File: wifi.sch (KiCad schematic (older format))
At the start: 5 parts

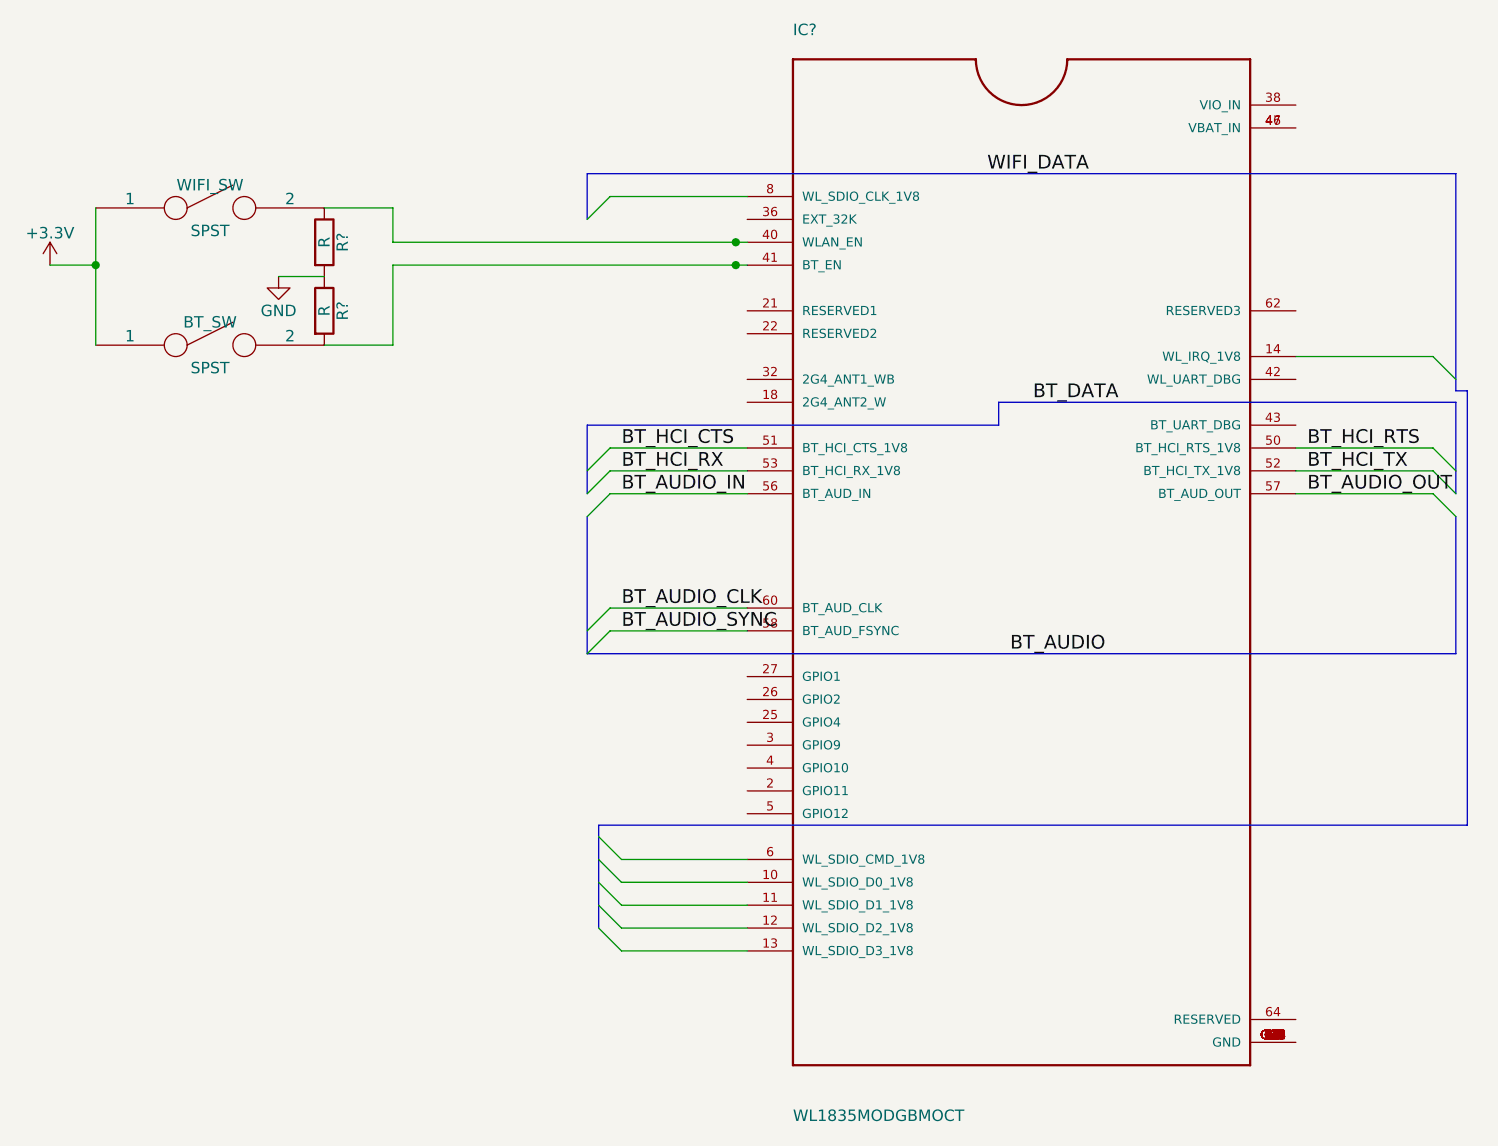
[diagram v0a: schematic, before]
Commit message: modular concept sketch
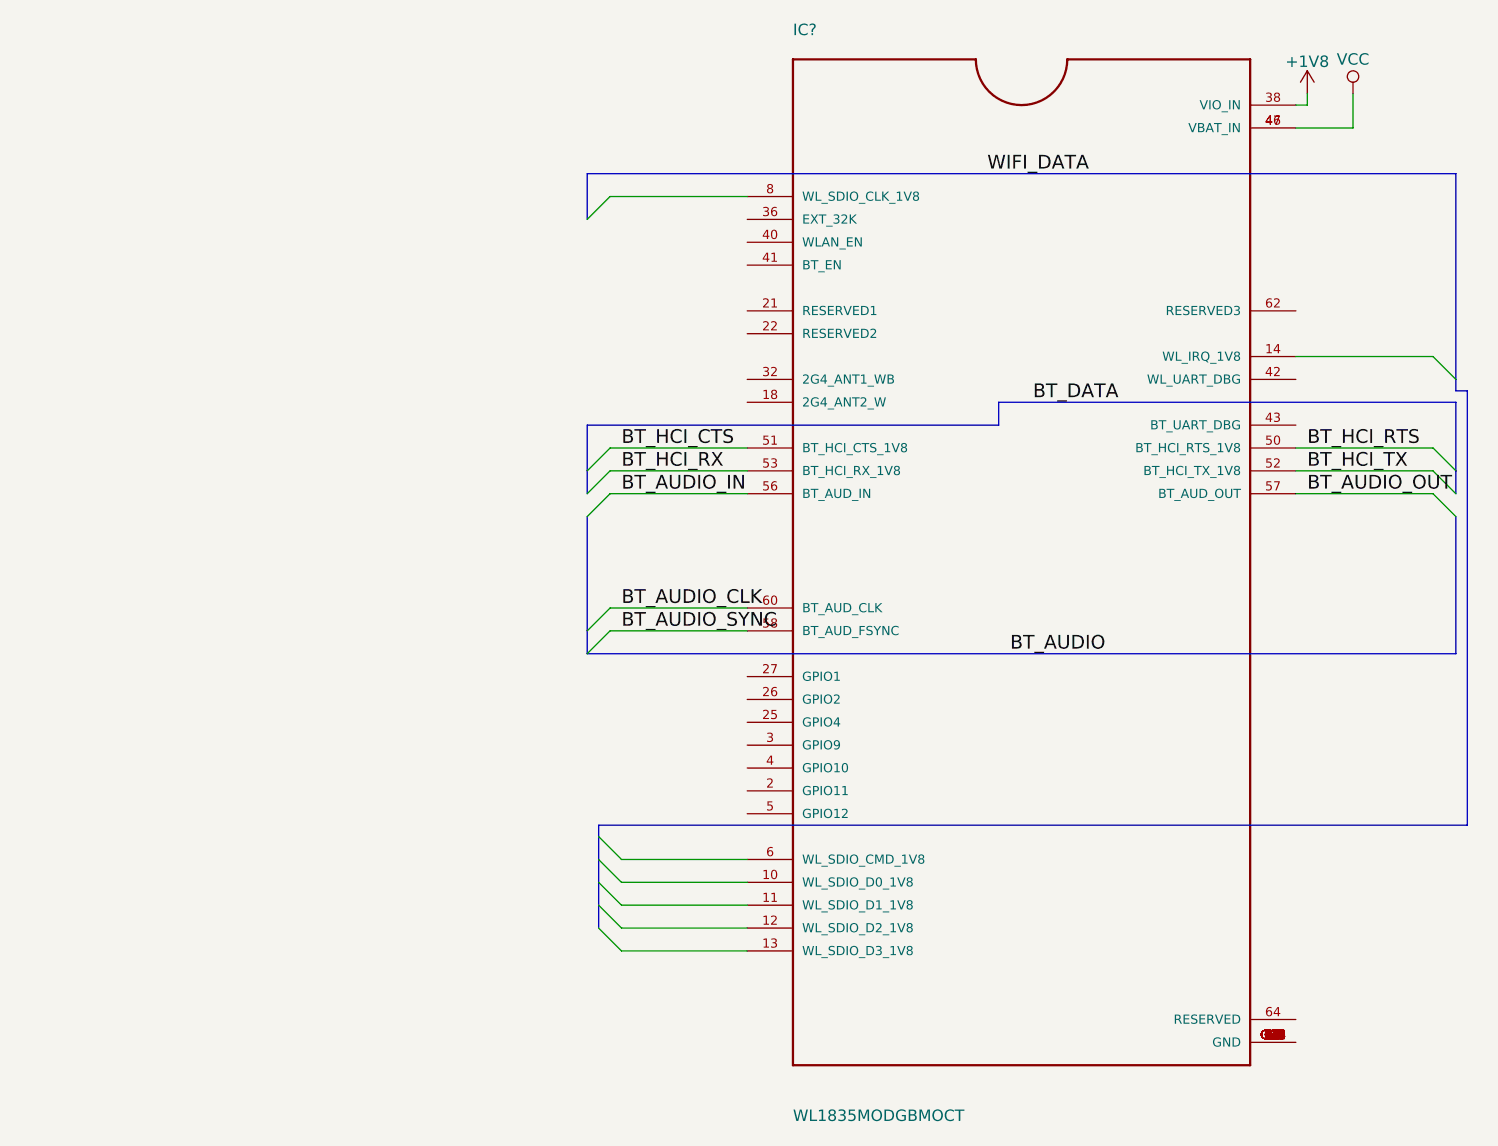
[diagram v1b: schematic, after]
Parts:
- removed BT_SW, WIFI_SW: SPST, symbol SPST
- removed R? (x2): R, symbol R
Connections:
- net +1V8: now reaches IC?.38 (VIO_IN)
- net VCC: now reaches IC?.46 (VBAT_IN), IC?.47 (VBAT_IN)
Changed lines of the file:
@@
 Comment4 ""
 $EndDescr
-$Comp
-L WL1835MODGBMOCT IC?
-U 1 1 59398D7D
-P 5500 3550
-F 0 "IC?" H 4500 5750 50  0000 L BNN
-F 1 "WL1835MODGBMOCT" H 4500 1000 50  0000 L BNN
-F 2 "MOC-100" H 5500 3550 50  0001 L BNN
-F 3 "None" H 5500 3550 50  0001 L BNN
-F 4 "WL1835MODGBMOCT" H 5500 3550 50  0001 L BNN "MP"
-F 5 "Texas Instruments" H 5500 3550 50  0001 L BNN "MF"
-F 6 "Module 802.11b/g/n 100000Kbps 100-Pin SIP SMD Module" H 5500 3550 50  0001 L BNN "Description"
-F 7 "Good" H 5500 3550 50  0001 L BNN "Availability"
-F 8 "19.86 USD" H 5500 3550 50  0001 L BNN "Price"
-	1    5500 3550
-	1    0    0    -1
-$EndComp
-$Comp
-L SPST WIFI_SW
-U 1 1 59398EF7
-P 1950 2100
-F 0 "WIFI_SW" H 1950 2200 50  0000 C CNN
-F 1 "SPST" H 1950 2000 50  0000 C CNN
-F 2 "" H 1950 2100 50  0000 C CNN
-F 3 "" H 1950 2100 50  0000 C CNN
-	1    1950 2100
-	1    0    0    -1
-$EndComp
-$Comp
-L SPST BT_SW
-U 1 1 59399006
-P 1950 2700
-F 0 "BT_SW" H 1950 2800 50  0000 C CNN
-F 1 "SPST" H 1950 2600 50  0000 C CNN
-F 2 "" H 1950 2700 50  0000 C CNN
-F 3 "" H 1950 2700 50  0000 C CNN
-	1    1950 2700
-	1    0    0    -1
-$EndComp
-Wire Wire Line
-	2450 2100 2750 2100
-Wire Wire Line
-	2750 2250 4300 2250
-Wire Wire Line
-	2750 2350 4300 2350
-Wire Wire Line
-	2750 2700 2450 2700
-$Comp
-L R R?
-U 1 1 59399437
-P 2450 2250
-F 0 "R?" V 2530 2250 50  0000 C CNN
-F 1 "R" V 2450 2250 50  0000 C CNN
-F 2 "" V 2380 2250 50  0000 C CNN
-F 3 "" H 2450 2250 50  0000 C CNN
-	1    2450 2250
-	1    0    0    -1
-$EndComp
-$Comp
-L R R?
-U 1 1 593994C0
-P 2450 2550
-F 0 "R?" V 2530 2550 50  0000 C CNN
-F 1 "R" V 2450 2550 50  0000 C CNN
-F 2 "" V 2380 2550 50  0000 C CNN
-F 3 "" H 2450 2550 50  0000 C CNN
-	1    2450 2550
-	1    0    0    -1
-$EndComp
-Wire Wire Line
-	2450 2400 2250 2400
-$Comp
-L GND #PWR?
-U 1 1 5939963D
-P 2250 2400
-F 0 "#PWR?" H 2250 2150 50  0001 C CNN
-F 1 "GND" H 2250 2250 50  0000 C CNN
-F 2 "" H 2250 2400 50  0000 C CNN
-F 3 "" H 2250 2400 50  0000 C CNN
-	1    2250 2400
-	1    0    0    -1
-$EndComp
-Wire Wire Line
-	1450 2100 1450 2700
-$Comp
-L +3.3V #PWR?
-U 1 1 5939966F
-P 1250 2350
-F 0 "#PWR?" H 1250 2200 50  0001 C CNN
-F 1 "+3.3V" H 1250 2490 50  0000 C CNN
-F 2 "" H 1250 2350 50  0000 C CNN
-F 3 "" H 1250 2350 50  0000 C CNN
-	1    1250 2350
-	1    0    0    -1
-$EndComp
-Wire Wire Line
-	1250 2350 1450 2350
-Connection ~ 1450 2350
-Wire Wire Line
-	2750 2100 2750 2250
-Connection ~ 4250 2250
-Wire Wire Line
-	2750 2350 2750 2700
-Connection ~ 4250 2350
 Wire Wire Line
 	3750 4950 4300 4950
@@
 BT_AUDIO_CLK
 Wire Bus Line
-	3600 3450 3600 4050
+	3600 3450 3600 3950
+Wire Bus Line
+	3600 3950 3600 4050
 Wire Bus Line
 	3600 4050 7400 4050
@@
 	7300 3150 7400 3250
 Wire Bus Line
-	7400 3350 7400 2950
+	7400 3350 7400 3250
+Wire Bus Line
+	7400 3250 7400 2950
 Wire Bus Line
 	7400 2950 5400 2950
@@
 	5400 3050 3600 3050
 Wire Bus Line
-	3600 3050 3600 3350
+	3600 3050 3600 3250
+Wire Bus Line
+	3600 3250 3600 3350
 Text Label 5450 4050 0    60   ~ 0
 BT_AUDIO
@@
 	3650 5250 3750 5350
 Wire Bus Line
-	3650 5250 3650 4800
+	3650 5250 3650 5150
+Wire Bus Line
+	3650 5150 3650 5050
+Wire Bus Line
+	3650 5050 3650 4950
+Wire Bus Line
+	3650 4950 3650 4850
+Wire Bus Line
+	3650 4850 3650 4800
 Wire Bus Line
 	3650 4800 7450 4800
@@
 	7450 2900 7400 2900
 Wire Bus Line
-	7400 2900 7400 1950
+	7400 2900 7400 2850
+Wire Bus Line
+	7400 2850 7400 1950
 Wire Bus Line
 	7400 1950 3600 1950
@@
 Text Label 5350 1950 0    60   ~ 0
 WIFI_DATA
+$Comp
+L +1V8 #PWR?
+U 1 1 593B1302
+P 6750 1600
+F 0 "#PWR?" H 6750 1450 50  0001 C CNN
+F 1 "+1V8" H 6750 1740 50  0000 C CNN
+F 2 "" H 6750 1600 50  0000 C CNN
+F 3 "" H 6750 1600 50  0000 C CNN
+	1    6750 1600
+	1    0    0    -1
+$EndComp
+Wire Wire Line
+	6700 1650 6750 1650
+Wire Wire Line
+	6750 1650 6750 1600
+$Comp
+L VCC #PWR?
+U 1 1 593B14F2
+P 6950 1600
+F 0 "#PWR?" H 6950 1450 50  0001 C CNN
+F 1 "VCC" H 6950 1750 50  0000 C CNN
+F 2 "" H 6950 1600 50  0000 C CNN
+F 3 "" H 6950 1600 50  0000 C CNN
+	1    6950 1600
+	1    0    0    -1
+$EndComp
+Wire Wire Line
+	6700 1750 6950 1750
+Wire Wire Line
+	6950 1750 6950 1600
+$Comp
+L WL1835MODGBMOCT IC?
+U 1 1 59398D7D
+P 5500 3550
+F 0 "IC?" H 4500 5750 50  0000 L BNN
+F 1 "WL1835MODGBMOCT" H 4500 1000 50  0000 L BNN
+F 2 "MOC-100" H 5500 3550 50  0001 L BNN
+F 3 "None" H 5500 3550 50  0001 L BNN
+F 4 "WL1835MODGBMOCT" H 5500 3550 50  0001 L BNN "MP"
+F 5 "Texas Instruments" H 5500 3550 50  0001 L BNN "MF"
+F 6 "Module 802.11b/g/n 100000Kbps 100-Pin SIP SMD Module" H 5500 3550 50  0001 L BNN "Description"
+F 7 "Good" H 5500 3550 50  0001 L BNN "Availability"
+F 8 "19.86 USD" H 5500 3550 50  0001 L BNN "Price"
+	1    5500 3550
+	1    0    0    -1
+$EndComp
 $EndSCHEMATC
